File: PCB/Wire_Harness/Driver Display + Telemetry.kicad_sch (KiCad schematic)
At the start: 2 parts, among them J13 Motor Controller 12-pin, J14 Motor Controller 20-pin

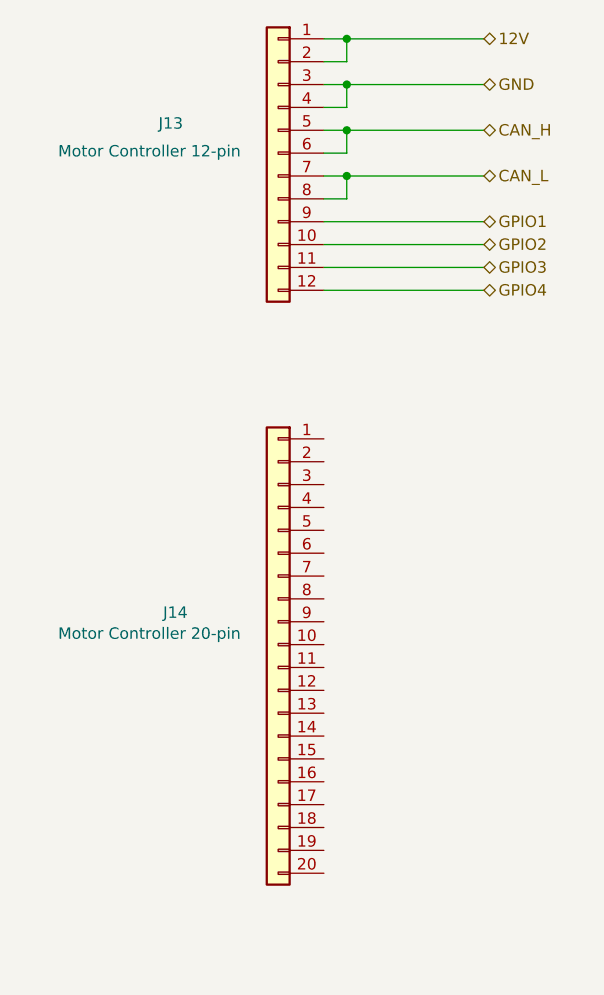
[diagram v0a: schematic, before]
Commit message: changed schematic size to 11x17, added part numbers for enclosures and connectors
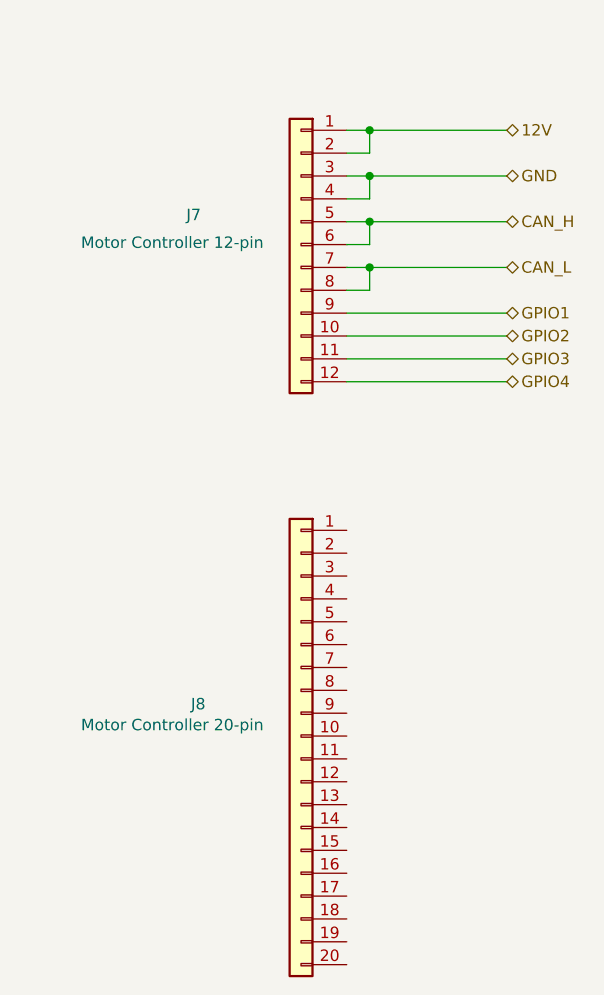
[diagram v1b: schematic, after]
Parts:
- removed J13: Motor Controller 12-pin, symbol VMS_Symbols:Conn_01x12
- removed J14: Motor Controller 20-pin, symbol VMS_Symbols:Conn_01x20
- added J7: Motor Controller 12-pin, symbol VMS_Symbols:Conn_01x12
- added J8: Motor Controller 20-pin, symbol VMS_Symbols:Conn_01x20
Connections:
- net 12V: now also J7.1 (Pin_1), J7.2 (Pin_2)
- net CAN_H: now also J7.5 (Pin_5), J7.6 (Pin_6)
- net CAN_L: now also J7.7 (Pin_7), J7.8 (Pin_8)
- net GND: now also J7.3 (Pin_3), J7.4 (Pin_4)
- net GPIO1: now also J7.9 (Pin_9)
- net GPIO2: now also J7.10 (Pin_10)
- net GPIO3: now also J7.11 (Pin_11)
- net GPIO4: now also J7.12 (Pin_12)
